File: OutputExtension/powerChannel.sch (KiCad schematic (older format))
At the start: 2 parts, among them Q1 IRL640

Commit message: Output extension looks good. Diodes still missing
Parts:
- added Q2: BSS138, Package_TO_SOT_SMD:SOT-23, symbol Device:Q_NMOS_GSD
- added Q3: 35N15, Package_TO_SOT_SMD:TO-263-3_TabPin2, symbol OutputExtension-rescue:Q_NMOS_GDS-OutputExtension-rescue
- Q1: footprint TO_SOT_Packages_THT:TO-220_Neutral123_Vertical_LargePads -> Package_TO_SOT_THT:TO-220-3_Vertical; symbol Q_NMOS_GDS -> OutputExtension-rescue:Q_NMOS_GDS-OutputExtension-rescue
- R3: symbol R -> OutputExtension-rescue:R-OutputExtension-rescue
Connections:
- wire segments 7 -> 20
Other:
- note added: "DNP"
- moved on the sheet: R10
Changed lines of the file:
@@
-EESchema Schematic File Version 2
-LIBS:power
-LIBS:device
-LIBS:transistors
-LIBS:conn
-LIBS:linear
-LIBS:regul
-LIBS:74xx
-LIBS:cmos4000
-LIBS:adc-dac
-LIBS:memory
-LIBS:xilinx
-LIBS:microcontrollers
-LIBS:dsp
-LIBS:microchip
-LIBS:analog_switches
-LIBS:motorola
-LIBS:texas
-LIBS:intel
-LIBS:audio
-LIBS:interface
-LIBS:digital-audio
-LIBS:philips
-LIBS:display
-LIBS:cypress
-LIBS:siliconi
-LIBS:opto
-LIBS:atmel
-LIBS:contrib
-LIBS:valves
-LIBS:fan_tas_tic-cache
-EELAYER 25 0
+EESchema Schematic File Version 4
+LIBS:OutputExtension-cache
+EELAYER 26 0
 EELAYER END
 $Descr A4 11693 8268
 encoding utf-8
-Sheet 2 9
+Sheet 3 9
 Title ""
 Date ""
@@
 Comment4 ""
 $EndDescr
-Text HLabel 1850 3600 0    60   Input ~ 0
+Text HLabel 1800 3750 0    60   Input ~ 0
 CTRL
 Text HLabel 1800 4700 0    60   UnSpc ~ 0
 GND
-Text HLabel 5150 3600 2    60   Output ~ 0
+Text HLabel 6000 3600 2    60   Output ~ 0
 DRAIN
 Wire Wire Line
-	1800 4700 5400 4700
+	1800 4700 4600 4700
 Wire Wire Line
-	4600 4200 4600 4700
+	4600 4200 4600 4400
 Connection ~ 4600 4700
 Wire Wire Line
@@
 	4600 3600 5150 3600
 Wire Wire Line
-	4300 3600 4300 4000
+	4300 3750 4300 4000
 $Comp
-L R R3
+L OutputExtension-rescue:R-OutputExtension-rescue R3
 U 1 1 567075BF
-P 3000 3600
+P 3000 3750
 AR Path="/568473CE/567075BF" Ref="R3"  Part="1"
-AR Path="/568473CF/567075BF" Ref="R4"  Part="1"
-AR Path="/568473D0/567075BF" Ref="R5"  Part="1"
-AR Path="/568473D1/567075BF" Ref="R6"  Part="1"
-AR Path="/568473D8/567075BF" Ref="R7"  Part="1"
-AR Path="/568473D9/567075BF" Ref="R8"  Part="1"
-AR Path="/568473DA/567075BF" Ref="R9"  Part="1"
-AR Path="/568473DB/567075BF" Ref="R10"  Part="1"
-F 0 "R10" V 3080 3600 50  0000 C CNN
-F 1 "470R" V 3000 3600 50  0000 C CNN
-F 2 "Resistors_SMD:R_0805_HandSoldering" V 2930 3600 50  0001 C CNN
-F 3 "" H 3000 3600 50  0000 C CNN
-	1    3000 3600
+AR Path="/568473CF/567075BF" Ref="R?"  Part="1"
+AR Path="/568473D0/567075BF" Ref="R?"  Part="1"
+AR Path="/568473D1/567075BF" Ref="R?"  Part="1"
+AR Path="/568473D8/567075BF" Ref="R?"  Part="1"
+AR Path="/568473D9/567075BF" Ref="R?"  Part="1"
+AR Path="/568473DA/567075BF" Ref="R?"  Part="1"
+AR Path="/568473DB/567075BF" Ref="R?"  Part="1"
+AR Path="/567075BF" Ref="R?"  Part="1"
+AR Path="/5BF99CAF/567075BF" Ref="R4"  Part="1"
+AR Path="/5BFA00DD/567075BF" Ref="R5"  Part="1"
+AR Path="/5BFA64DD/567075BF" Ref="R6"  Part="1"
+AR Path="/5BFACA74/567075BF" Ref="R7"  Part="1"
+AR Path="/5BFACA79/567075BF" Ref="R8"  Part="1"
+AR Path="/5BFACA7E/567075BF" Ref="R9"  Part="1"
+AR Path="/5BFACA83/567075BF" Ref="R10"  Part="1"
+F 0 "R10" V 3080 3750 50  0000 C CNN
+F 1 "470R" V 3000 3750 50  0000 C CNN
+F 2 "Resistors_SMD:R_0805_HandSoldering" V 2930 3750 50  0001 C CNN
+F 3 "" H 3000 3750 50  0000 C CNN
+	1    3000 3750
 	0    1    1    0
 $EndComp
 Wire Wire Line
-	1850 3600 2850 3600
+	1800 3750 2850 3750
 Wire Wire Line
-	3150 3600 4300 3600
+	3150 3750 4300 3750
 $Comp
-L Q_NMOS_GDS Q1
+L OutputExtension-rescue:Q_NMOS_GDS-OutputExtension-rescue Q1
 U 1 1 56763CC0
 P 4500 4000
 AR Path="/568473CE/56763CC0" Ref="Q1"  Part="1"
-AR Path="/568473CF/56763CC0" Ref="Q2"  Part="1"
-AR Path="/568473D0/56763CC0" Ref="Q3"  Part="1"
-AR Path="/568473D1/56763CC0" Ref="Q4"  Part="1"
-AR Path="/568473D8/56763CC0" Ref="Q5"  Part="1"
-AR Path="/568473D9/56763CC0" Ref="Q6"  Part="1"
-AR Path="/568473DA/56763CC0" Ref="Q7"  Part="1"
-AR Path="/568473DB/56763CC0" Ref="Q8"  Part="1"
-F 0 "Q8" H 4800 4050 50  0000 R CNN
-F 1 "IRL640" H 5150 3950 50  0000 R CNN
-F 2 "TO_SOT_Packages_THT:TO-220_Neutral123_Vertical_LargePads" H 4700 4100 50  0001 C CNN
+AR Path="/568473CF/56763CC0" Ref="Q?"  Part="1"
+AR Path="/568473D0/56763CC0" Ref="Q?"  Part="1"
+AR Path="/568473D1/56763CC0" Ref="Q?"  Part="1"
+AR Path="/568473D8/56763CC0" Ref="Q?"  Part="1"
+AR Path="/568473D9/56763CC0" Ref="Q?"  Part="1"
+AR Path="/568473DA/56763CC0" Ref="Q?"  Part="1"
+AR Path="/568473DB/56763CC0" Ref="Q?"  Part="1"
+AR Path="/56763CC0" Ref="Q?"  Part="1"
+AR Path="/5BF99CAF/56763CC0" Ref="Q4"  Part="1"
+AR Path="/5BFA00DD/56763CC0" Ref="Q7"  Part="1"
+AR Path="/5BFA64DD/56763CC0" Ref="Q10"  Part="1"
+AR Path="/5BFACA74/56763CC0" Ref="Q13"  Part="1"
+AR Path="/5BFACA79/56763CC0" Ref="Q16"  Part="1"
+AR Path="/5BFACA7E/56763CC0" Ref="Q19"  Part="1"
+AR Path="/5BFACA83/56763CC0" Ref="Q22"  Part="1"
+F 0 "Q22" H 4800 4050 50  0000 R CNN
+F 1 "IRL640" V 4500 3800 50  0000 R CNN
+F 2 "Package_TO_SOT_THT:TO-220-3_Vertical" H 4700 4100 50  0001 C CNN
 F 3 "" H 4500 4000 50  0000 C CNN
 	1    4500 4000
 	1    0    0    -1
 $EndComp
+$Comp
+L Device:Q_NMOS_GSD Q2
+U 1 1 5BEE0A74
+P 5050 4000
+AR Path="/568473CE/5BEE0A74" Ref="Q2"  Part="1"
+AR Path="/568473CF/5BEE0A74" Ref="Q?"  Part="1"
+AR Path="/568473D0/5BEE0A74" Ref="Q?"  Part="1"
+AR Path="/568473D1/5BEE0A74" Ref="Q?"  Part="1"
+AR Path="/568473D8/5BEE0A74" Ref="Q?"  Part="1"
+AR Path="/568473D9/5BEE0A74" Ref="Q?"  Part="1"
+AR Path="/568473DA/5BEE0A74" Ref="Q?"  Part="1"
+AR Path="/568473DB/5BEE0A74" Ref="Q?"  Part="1"
+AR Path="/5BF99CAF/5BEE0A74" Ref="Q5"  Part="1"
+AR Path="/5BFA00DD/5BEE0A74" Ref="Q8"  Part="1"
+AR Path="/5BFA64DD/5BEE0A74" Ref="Q11"  Part="1"
+AR Path="/5BFACA74/5BEE0A74" Ref="Q14"  Part="1"
+AR Path="/5BFACA79/5BEE0A74" Ref="Q17"  Part="1"
+AR Path="/5BFACA7E/5BEE0A74" Ref="Q20"  Part="1"
+AR Path="/5BFACA83/5BEE0A74" Ref="Q23"  Part="1"
+F 0 "Q23" H 5255 4046 50  0000 L CNN
+F 1 "BSS138" V 5250 3450 50  0000 L CNN
+F 2 "Package_TO_SOT_SMD:SOT-23" H 5250 4100 50  0001 C CNN
+F 3 "~" H 5050 4000 50  0001 C CNN
+	1    5050 4000
+	1    0    0    -1
+$EndComp
+Wire Wire Line
+	5150 3800 5150 3600
+Connection ~ 5150 3600
+Wire Wire Line
+	5150 3600 5850 3600
+Wire Wire Line
+	5150 4200 5150 4400
+Wire Wire Line
+	5150 4400 4600 4400
+Connection ~ 4600 4400
+Wire Wire Line
+	4600 4400 4600 4700
+Wire Wire Line
+	4300 3750 4850 3750
+Wire Wire Line
+	4850 3750 4850 4000
+Connection ~ 4300 3750
+Text Notes 5250 4150 0    50   ~ 0
+DNP
+$Comp
+L OutputExtension-rescue:Q_NMOS_GDS-OutputExtension-rescue Q3
+U 1 1 5BFB3710
+P 5750 4000
+AR Path="/568473CE/5BFB3710" Ref="Q3"  Part="1"
+AR Path="/568473CF/5BFB3710" Ref="Q?"  Part="1"
+AR Path="/568473D0/5BFB3710" Ref="Q?"  Part="1"
+AR Path="/568473D1/5BFB3710" Ref="Q?"  Part="1"
+AR Path="/568473D8/5BFB3710" Ref="Q?"  Part="1"
+AR Path="/568473D9/5BFB3710" Ref="Q?"  Part="1"
+AR Path="/568473DA/5BFB3710" Ref="Q?"  Part="1"
+AR Path="/568473DB/5BFB3710" Ref="Q?"  Part="1"
+AR Path="/5BFB3710" Ref="Q?"  Part="1"
+AR Path="/5BF99CAF/5BFB3710" Ref="Q6"  Part="1"
+AR Path="/5BFA00DD/5BFB3710" Ref="Q9"  Part="1"
+AR Path="/5BFA64DD/5BFB3710" Ref="Q12"  Part="1"
+AR Path="/5BFACA74/5BFB3710" Ref="Q15"  Part="1"
+AR Path="/5BFACA79/5BFB3710" Ref="Q18"  Part="1"
+AR Path="/5BFACA7E/5BFB3710" Ref="Q21"  Part="1"
+AR Path="/5BFACA83/5BFB3710" Ref="Q24"  Part="1"
+F 0 "Q24" H 6050 4050 50  0000 R CNN
+F 1 "35N15" V 5750 3800 50  0000 R CNN
+F 2 "Package_TO_SOT_SMD:TO-263-3_TabPin2" H 5950 4100 50  0001 C CNN
+F 3 "" H 5750 4000 50  0000 C CNN
+	1    5750 4000
+	1    0    0    -1
+$EndComp
+Wire Wire Line
+	4850 3750 5550 3750
+Wire Wire Line
+	5550 3750 5550 4000
+Connection ~ 4850 3750
+Wire Wire Line
+	5850 3800 5850 3600
+Connection ~ 5850 3600
+Wire Wire Line
+	5850 3600 6000 3600
+Wire Wire Line
+	5850 4200 5850 4700
+Wire Wire Line
+	4600 4700 5850 4700
 $EndSCHEMATC

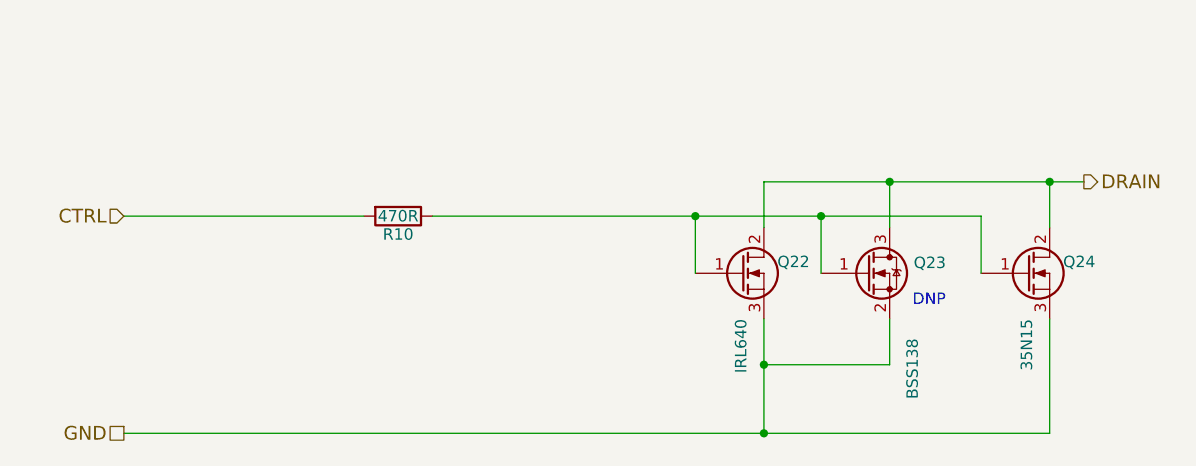
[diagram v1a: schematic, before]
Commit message: Add diodes
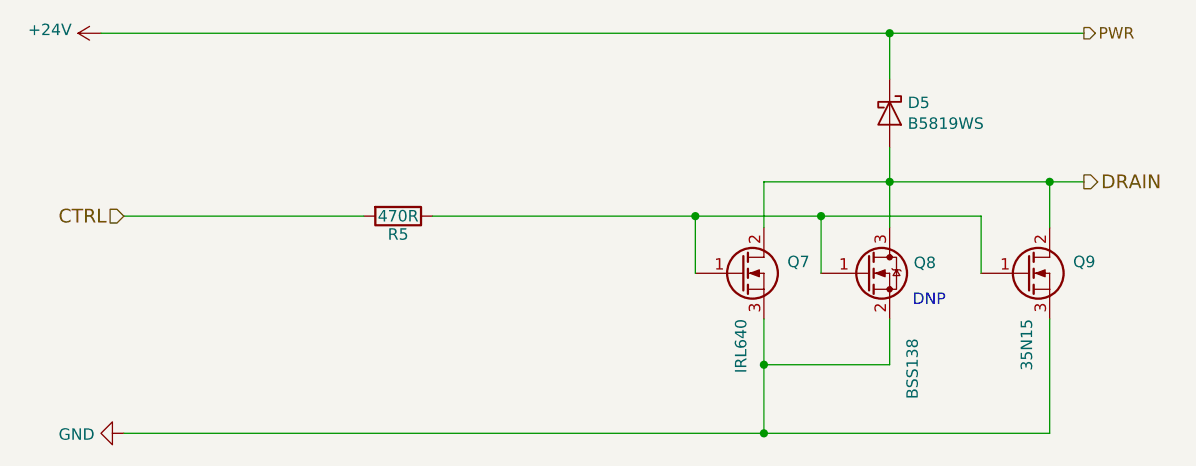
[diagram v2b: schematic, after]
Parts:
- added D3: B5819WS, Diode_SMD:D_SOD-323, symbol Device:D_Schottky
- R3: footprint Resistors_SMD:R_0805_HandSoldering -> Resistor_SMD:R_0805_2012Metric
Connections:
- net DRAIN: now also D3.2 (A)
- new net +24V: D3.1 (K)
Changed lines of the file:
@@
 $Descr A4 11693 8268
 encoding utf-8
-Sheet 3 9
+Sheet 2 9
 Title ""
 Date ""
@@
 Text HLabel 1800 3750 0    60   Input ~ 0
 CTRL
-Text HLabel 1800 4700 0    60   UnSpc ~ 0
-GND
 Text HLabel 6000 3600 2    60   Output ~ 0
 DRAIN
@@
 AR Path="/5BFACA7E/567075BF" Ref="R9"  Part="1"
 AR Path="/5BFACA83/567075BF" Ref="R10"  Part="1"
-F 0 "R10" V 3080 3750 50  0000 C CNN
+F 0 "R5" V 3080 3750 50  0000 C CNN
 F 1 "470R" V 3000 3750 50  0000 C CNN
-F 2 "Resistors_SMD:R_0805_HandSoldering" V 2930 3750 50  0001 C CNN
+F 2 "Resistor_SMD:R_0805_2012Metric" V 2930 3750 50  0001 C CNN
 F 3 "" H 3000 3750 50  0000 C CNN
 	1    3000 3750
@@
 AR Path="/5BFACA7E/56763CC0" Ref="Q19"  Part="1"
 AR Path="/5BFACA83/56763CC0" Ref="Q22"  Part="1"
-F 0 "Q22" H 4800 4050 50  0000 R CNN
+F 0 "Q7" H 4800 4050 50  0000 R CNN
 F 1 "IRL640" V 4500 3800 50  0000 R CNN
 F 2 "Package_TO_SOT_THT:TO-220-3_Vertical" H 4700 4100 50  0001 C CNN
@@
 AR Path="/5BFACA7E/5BEE0A74" Ref="Q20"  Part="1"
 AR Path="/5BFACA83/5BEE0A74" Ref="Q23"  Part="1"
-F 0 "Q23" H 5255 4046 50  0000 L CNN
+F 0 "Q8" H 5255 4046 50  0000 L CNN
 F 1 "BSS138" V 5250 3450 50  0000 L CNN
 F 2 "Package_TO_SOT_SMD:SOT-23" H 5250 4100 50  0001 C CNN
@@
 AR Path="/5BFACA7E/5BFB3710" Ref="Q21"  Part="1"
 AR Path="/5BFACA83/5BFB3710" Ref="Q24"  Part="1"
-F 0 "Q24" H 6050 4050 50  0000 R CNN
+F 0 "Q9" H 6050 4050 50  0000 R CNN
 F 1 "35N15" V 5750 3800 50  0000 R CNN
 F 2 "Package_TO_SOT_SMD:TO-263-3_TabPin2" H 5950 4100 50  0001 C CNN
@@
 Wire Wire Line
 	4600 4700 5850 4700
+$Comp
+L Device:D_Schottky D3
+U 1 1 5BECF7F4
+P 5150 3300
+AR Path="/568473CE/5BECF7F4" Ref="D3"  Part="1"
+AR Path="/5BF99CAF/5BECF7F4" Ref="D4"  Part="1"
+AR Path="/5BFA00DD/5BECF7F4" Ref="D5"  Part="1"
+AR Path="/5BFA64DD/5BECF7F4" Ref="D6"  Part="1"
+AR Path="/5BFACA74/5BECF7F4" Ref="D7"  Part="1"
+AR Path="/5BFACA79/5BECF7F4" Ref="D8"  Part="1"
+AR Path="/5BFACA7E/5BECF7F4" Ref="D9"  Part="1"
+AR Path="/5BFACA83/5BECF7F4" Ref="D10"  Part="1"
+F 0 "D5" V 5104 3379 50  0000 L CNN
+F 1 "B5819WS" V 5195 3379 50  0000 L CNN
+F 2 "Diode_SMD:D_SOD-323" H 5150 3300 50  0001 C CNN
+F 3 "~" H 5150 3300 50  0001 C CNN
+	1    5150 3300
+	0    1    1    0
+$EndComp
+Wire Wire Line
+	5150 3450 5150 3600
+Text HLabel 6000 2950 2    50   Output ~ 0
+PWR
+$Comp
+L power:+24V #PWR0103
+U 1 1 5BFB18DD
+P 1700 2950
+AR Path="/568473CE/5BFB18DD" Ref="#PWR0103"  Part="1"
+AR Path="/5BFA64DD/5BFB18DD" Ref="#PWR0105"  Part="1"
+AR Path="/5BFACA74/5BFB18DD" Ref="#PWR0107"  Part="1"
+AR Path="/5BFACA79/5BFB18DD" Ref="#PWR0109"  Part="1"
+AR Path="/5BFACA83/5BFB18DD" Ref="#PWR0111"  Part="1"
+AR Path="/5BF99CAF/5BFB18DD" Ref="#PWR0113"  Part="1"
+AR Path="/5BFA00DD/5BFB18DD" Ref="#PWR0115"  Part="1"
+AR Path="/5BFACA7E/5BFB18DD" Ref="#PWR0117"  Part="1"
+F 0 "#PWR0115" H 1700 2800 50  0001 C CNN
+F 1 "+24V" V 1715 3078 50  0000 L CNN
+F 2 "" H 1700 2950 50  0001 C CNN
+F 3 "" H 1700 2950 50  0001 C CNN
+	1    1700 2950
+	0    -1   -1   0
+$EndComp
+Wire Wire Line
+	5150 2950 5150 3150
+Connection ~ 5150 2950
+Wire Wire Line
+	5150 2950 6000 2950
+Wire Wire Line
+	1700 2950 5150 2950
+$Comp
+L power:GND #PWR0104
+U 1 1 5BFEA3D2
+P 1800 4700
+AR Path="/568473CE/5BFEA3D2" Ref="#PWR0104"  Part="1"
+AR Path="/5BFA64DD/5BFEA3D2" Ref="#PWR0106"  Part="1"
+AR Path="/5BFACA74/5BFEA3D2" Ref="#PWR0108"  Part="1"
+AR Path="/5BFACA79/5BFEA3D2" Ref="#PWR0110"  Part="1"
+AR Path="/5BFACA83/5BFEA3D2" Ref="#PWR0112"  Part="1"
+AR Path="/5BF99CAF/5BFEA3D2" Ref="#PWR0114"  Part="1"
+AR Path="/5BFA00DD/5BFEA3D2" Ref="#PWR0116"  Part="1"
+AR Path="/5BFACA7E/5BFEA3D2" Ref="#PWR0118"  Part="1"
+F 0 "#PWR0116" H 1800 4450 50  0001 C CNN
+F 1 "GND" V 1805 4572 50  0000 R CNN
+F 2 "" H 1800 4700 50  0001 C CNN
+F 3 "" H 1800 4700 50  0001 C CNN
+	1    1800 4700
+	0    1    1    0
+$EndComp
 $EndSCHEMATC

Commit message: Fabbed version
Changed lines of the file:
@@
 AR Path="/5BFACA7E/567075BF" Ref="R9"  Part="1"
 AR Path="/5BFACA83/567075BF" Ref="R10"  Part="1"
-F 0 "R5" V 3080 3750 50  0000 C CNN
+F 0 "R9" V 3080 3750 50  0000 C CNN
 F 1 "470R" V 3000 3750 50  0000 C CNN
 F 2 "Resistor_SMD:R_0805_2012Metric" V 2930 3750 50  0001 C CNN
@@
 AR Path="/5BFACA7E/56763CC0" Ref="Q19"  Part="1"
 AR Path="/5BFACA83/56763CC0" Ref="Q22"  Part="1"
-F 0 "Q7" H 4800 4050 50  0000 R CNN
+F 0 "Q19" H 4800 4050 50  0000 R CNN
 F 1 "IRL640" V 4500 3800 50  0000 R CNN
 F 2 "Package_TO_SOT_THT:TO-220-3_Vertical" H 4700 4100 50  0001 C CNN
@@
 AR Path="/5BFACA7E/5BEE0A74" Ref="Q20"  Part="1"
 AR Path="/5BFACA83/5BEE0A74" Ref="Q23"  Part="1"
-F 0 "Q8" H 5255 4046 50  0000 L CNN
+F 0 "Q20" H 5255 4046 50  0000 L CNN
 F 1 "BSS138" V 5250 3450 50  0000 L CNN
 F 2 "Package_TO_SOT_SMD:SOT-23" H 5250 4100 50  0001 C CNN
@@
 AR Path="/5BFACA7E/5BFB3710" Ref="Q21"  Part="1"
 AR Path="/5BFACA83/5BFB3710" Ref="Q24"  Part="1"
-F 0 "Q9" H 6050 4050 50  0000 R CNN
+F 0 "Q21" H 6050 4050 50  0000 R CNN
 F 1 "35N15" V 5750 3800 50  0000 R CNN
 F 2 "Package_TO_SOT_SMD:TO-263-3_TabPin2" H 5950 4100 50  0001 C CNN
@@
 AR Path="/5BFACA7E/5BECF7F4" Ref="D9"  Part="1"
 AR Path="/5BFACA83/5BECF7F4" Ref="D10"  Part="1"
-F 0 "D5" V 5104 3379 50  0000 L CNN
+F 0 "D9" V 5104 3379 50  0000 L CNN
 F 1 "B5819WS" V 5195 3379 50  0000 L CNN
 F 2 "Diode_SMD:D_SOD-323" H 5150 3300 50  0001 C CNN
@@
 AR Path="/5BFA00DD/5BFB18DD" Ref="#PWR0115"  Part="1"
 AR Path="/5BFACA7E/5BFB18DD" Ref="#PWR0117"  Part="1"
-F 0 "#PWR0115" H 1700 2800 50  0001 C CNN
+F 0 "#PWR0117" H 1700 2800 50  0001 C CNN
 F 1 "+24V" V 1715 3078 50  0000 L CNN
 F 2 "" H 1700 2950 50  0001 C CNN
@@
 AR Path="/5BFA00DD/5BFEA3D2" Ref="#PWR0116"  Part="1"
 AR Path="/5BFACA7E/5BFEA3D2" Ref="#PWR0118"  Part="1"
-F 0 "#PWR0116" H 1800 4450 50  0001 C CNN
+F 0 "#PWR0118" H 1800 4450 50  0001 C CNN
 F 1 "GND" V 1805 4572 50  0000 R CNN
 F 2 "" H 1800 4700 50  0001 C CNN

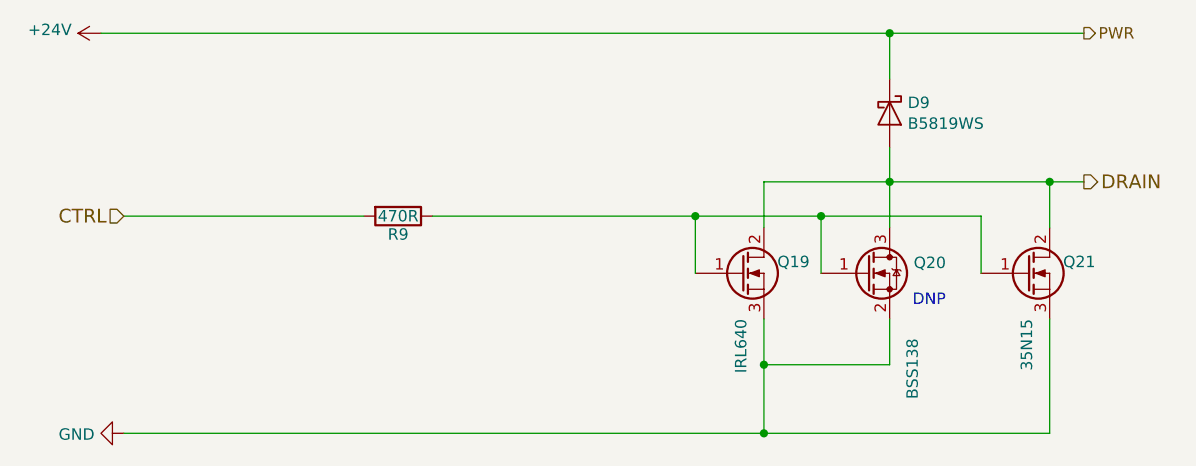
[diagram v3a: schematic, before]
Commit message: Output extension: chunkier freewheelingdiode
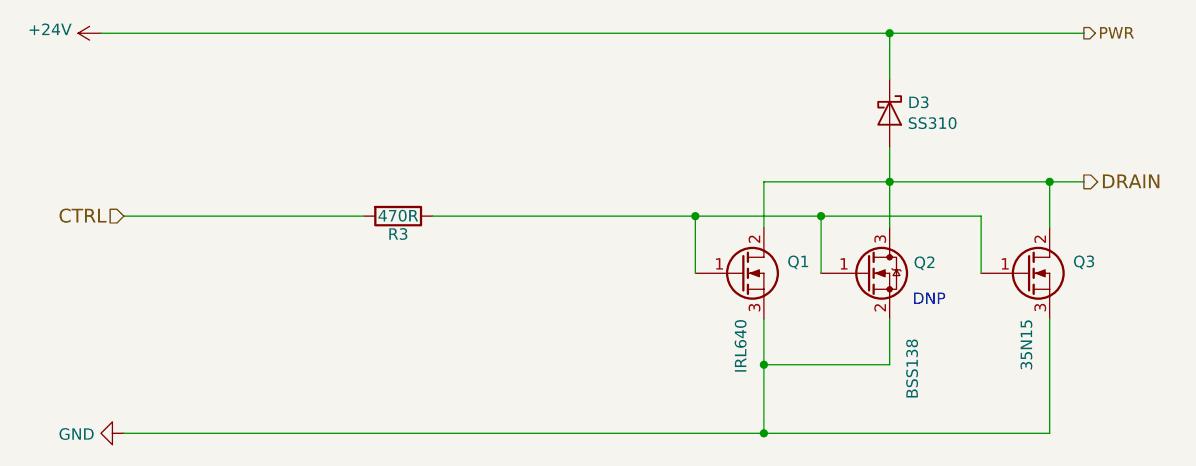
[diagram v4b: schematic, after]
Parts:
- D3: value B5819WS -> SS310; footprint Diode_SMD:D_SOD-323 -> Diode_SMD:D_SMC
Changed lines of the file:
@@
 Sheet 2 9
 Title ""
-Date ""
-Rev ""
+Date "2018-12-16"
+Rev "1"
 Comp ""
 Comment1 ""
@@
 AR Path="/5BFACA7E/567075BF" Ref="R9"  Part="1"
 AR Path="/5BFACA83/567075BF" Ref="R10"  Part="1"
-F 0 "R9" V 3080 3750 50  0000 C CNN
+F 0 "R3" V 3080 3750 50  0000 C CNN
 F 1 "470R" V 3000 3750 50  0000 C CNN
 F 2 "Resistor_SMD:R_0805_2012Metric" V 2930 3750 50  0001 C CNN
@@
 AR Path="/5BFACA7E/56763CC0" Ref="Q19"  Part="1"
 AR Path="/5BFACA83/56763CC0" Ref="Q22"  Part="1"
-F 0 "Q19" H 4800 4050 50  0000 R CNN
+F 0 "Q1" H 4800 4050 50  0000 R CNN
 F 1 "IRL640" V 4500 3800 50  0000 R CNN
 F 2 "Package_TO_SOT_THT:TO-220-3_Vertical" H 4700 4100 50  0001 C CNN
@@
 AR Path="/5BFACA7E/5BEE0A74" Ref="Q20"  Part="1"
 AR Path="/5BFACA83/5BEE0A74" Ref="Q23"  Part="1"
-F 0 "Q20" H 5255 4046 50  0000 L CNN
+F 0 "Q2" H 5255 4046 50  0000 L CNN
 F 1 "BSS138" V 5250 3450 50  0000 L CNN
 F 2 "Package_TO_SOT_SMD:SOT-23" H 5250 4100 50  0001 C CNN
@@
 AR Path="/5BFACA7E/5BFB3710" Ref="Q21"  Part="1"
 AR Path="/5BFACA83/5BFB3710" Ref="Q24"  Part="1"
-F 0 "Q21" H 6050 4050 50  0000 R CNN
+F 0 "Q3" H 6050 4050 50  0000 R CNN
 F 1 "35N15" V 5750 3800 50  0000 R CNN
 F 2 "Package_TO_SOT_SMD:TO-263-3_TabPin2" H 5950 4100 50  0001 C CNN
@@
 AR Path="/5BFACA7E/5BECF7F4" Ref="D9"  Part="1"
 AR Path="/5BFACA83/5BECF7F4" Ref="D10"  Part="1"
-F 0 "D9" V 5104 3379 50  0000 L CNN
-F 1 "B5819WS" V 5195 3379 50  0000 L CNN
-F 2 "Diode_SMD:D_SOD-323" H 5150 3300 50  0001 C CNN
+F 0 "D3" V 5104 3379 50  0000 L CNN
+F 1 "SS310" V 5195 3379 50  0000 L CNN
+F 2 "Diode_SMD:D_SMC" H 5150 3300 50  0001 C CNN
 F 3 "~" H 5150 3300 50  0001 C CNN
 	1    5150 3300
@@
 Connection ~ 5150 2950
 Wire Wire Line
-	5150 2950 6000 2950
-Wire Wire Line
 	1700 2950 5150 2950
 $Comp
@@
 	0    1    1    0
 $EndComp
+Wire Wire Line
+	5150 2950 6000 2950
 $EndSCHEMATC
